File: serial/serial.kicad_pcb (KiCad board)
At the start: 2 copper layers, 73.7 x 56.1 mm, 36 parts, among them J1 Conn_02x20_Odd_Even, J2 D-SUB Male 9 pins, U1 74LS30, U2 74LS02, U3 74LS00, U4 MC6850, U5 CD4060BE, U6 MAX232, Y1 4.0Mhz

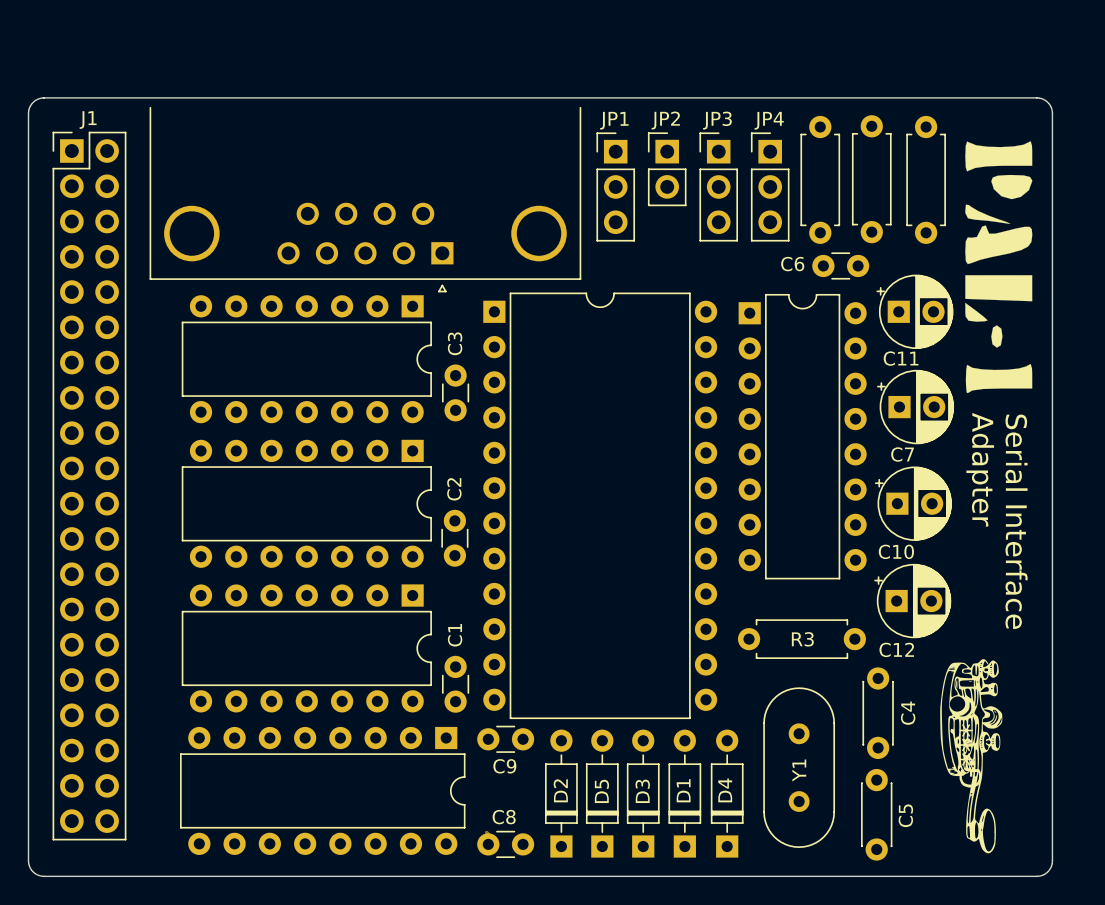
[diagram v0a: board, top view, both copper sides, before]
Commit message: Add TTL header
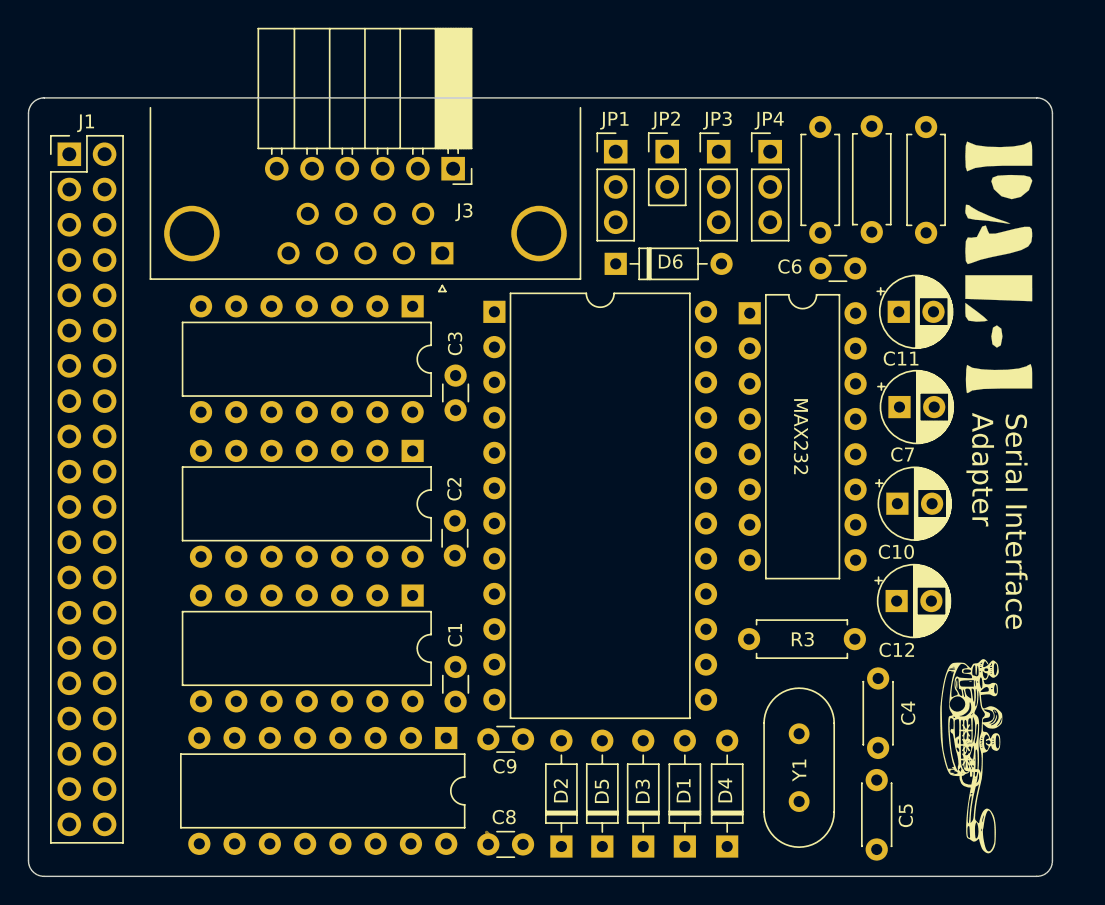
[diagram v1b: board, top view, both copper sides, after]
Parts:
- added D6: 1N4148, Diode_THT:D_DO-35_SOD27_P7.62mm_Horizontal, F.Cu at (142.0, 82.7)
- added J3: Conn_TTL, Connector_PinSocket_2.54mm:PinSocket_1x06_P2.54mm_Horizontal, F.Cu at (130.3, 75.9)
- moved J1 0.30 mm to (102.6, 74.8)
- moved C6 0.27 mm to (156.7, 83.0)
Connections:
- net Net-(U4-Pad2) renamed /Rx_D
- net Net-(U4-Pad24) renamed /CTS#
- net Net-(U4-Pad5) renamed /RTS#
- net Net-(U4-Pad6) renamed /Tx_D
- JP1 pad 2: A1 -> Net-(D6-Pad1)
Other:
- board text added: "MAX232"

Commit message: Minor improvements
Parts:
- removed D6: 1N4148, Diode_THT:D_DO-35_SOD27_P7.62mm_Horizontal
- removed the R2 at (160.4, 80.4)
- C7: renamed from C4; value 33p -> 33pF
- C8: renamed from C5; value 100p -> 100pF
- J3: value Conn_TTL -> Conn_01x06_Male; footprint Connector_PinSocket_2.54mm:PinSocket_1x06_P2.54mm_Horizontal -> Connector_PinHeader_2.54mm:PinHeader_1x06_P2.54mm_Horizontal
- U3: value 74LS00 -> 74LS02
- moved J3 13.1 mm to (117.2, 76.1), turned to 90 degrees
- moved U3 10.5 mm to (127.4, 96.2)
- moved U2 10.4 mm to (127.4, 85.8)
- moved R1 2.39 mm to (162.0, 80.4)
- moved R2 1.91 mm to (158.6, 80.4)
- moved JP1 0.49 mm to (142.3, 74.3)
- moved JP4 0.49 mm to (153.5, 74.3)
- moved JP2 0.49 mm to (146.1, 74.3)
- moved JP3 0.49 mm to (149.8, 74.3)
- moved U6 0.10 mm to (151.6, 86.2)
- renumbered C6 to C4, C9 to C5, C8 to C6, C7 to C9, R3 to R1, R4 to R2
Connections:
- J3 pad 2: /CTS# -> /RTS#
- J3 pad 4: /Tx_D -> /Rx_D
- J3 pad 5: /Rx_D -> /Tx_D
- J3 pad 6: /RTS# -> /CTS#
- JP1 pad 2: Net-(D6-Pad1) -> Net-(JP1-Pad2)
- JP1 pad 3: Net-(JP1-Pad3) -> A1
- U1 pad 1: Net-(JP1-Pad1) -> Net-(JP1-Pad2)
- U2 pad 2: Net-(JP1-Pad3) -> GND
- U3 pad 1: A6 -> Net-(U1-Pad6)
- U3 pad 10: A10 -> Net-(JP1-Pad1)
- U3 pad 11: Net-(U1-Pad11) -> GND
- U3 pad 12: Net-(U3-Pad12) -> GND
- U3 pad 13: Net-(U3-Pad12) -> unconnected-(U3-Pad13)
- U3 pad 2: A7 -> A6
- U3 pad 3: Net-(U3-Pad3) -> A7
- U3 pad 4: Net-(U3-Pad3) -> Net-(U1-Pad11)
- U3 pad 5: Net-(U3-Pad3) -> A9
- U3 pad 6: Net-(U1-Pad6) -> A10
- U3 pad 8: Net-(U3-Pad12) -> A1
- U3 pad 9: A9 -> A1

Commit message: Route pcb
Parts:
- removed the C7 at (160.9, 112.6)
- removed the C8 at (160.8, 124.9)
- removed the J2 at (129.5, 81.9)
- removed the R1 at (162.0, 80.4)
- removed the R1 at (159.2, 109.7)
- removed the U3 at (127.4, 96.2)
- added C12: 33pF, Capacitor_THT:C_Disc_D3.0mm_W1.6mm_P2.50mm, F.Cu at (130.1, 124.2)
- added C13: 33pF, Capacitor_THT:C_Disc_D3.0mm_W1.6mm_P2.50mm, F.Cu at (145.1, 121.6)
- added C4: 0.1uF, Capacitor_THT:C_Disc_D3.0mm_W1.6mm_P2.50mm, F.Cu at (128.0, 101.0)
- added D6: 1N4148, Diode_THT:D_DO-35_SOD27_P7.62mm_Horizontal, F.Cu at (155.2, 111.0)
- added J3: DB9_Male, Connector_Dsub:DSUB-9_Male_Horizontal_P2.77x2.84mm_EdgePinOffset7.70mm_Housed_MountingHolesOffset9.12mm, F.Cu at (129.2, 81.8)
- added R1: 2K2, Resistor_THT:R_Axial_DIN0207_L6.3mm_D2.5mm_P7.62mm_Horizontal, F.Cu at (141.4, 117.5)
- added R3: 2K7, Resistor_THT:R_Axial_DIN0207_L6.3mm_D2.5mm_P7.62mm_Horizontal, F.Cu at (130.6, 95.7)
- added R4: 2K2, Resistor_THT:R_Axial_DIN0207_L6.3mm_D2.5mm_P7.62mm_Horizontal, F.Cu at (130.6, 92.4)
- added R5: 2K2, Resistor_THT:R_Axial_DIN0207_L6.3mm_D2.5mm_P7.62mm_Horizontal, F.Cu at (130.6, 89.2)
- added R6: 2K2, Resistor_THT:R_Axial_DIN0207_L6.3mm_D2.5mm_P7.62mm_Horizontal, F.Cu at (130.6, 85.9)
- added R7: 2K2, Resistor_THT:R_Axial_DIN0207_L6.3mm_D2.5mm_P7.62mm_Horizontal, F.Cu at (132.3, 74.1)
- added U4: 74LS08, Package_DIP:DIP-14_W7.62mm, F.Cu at (124.5, 95.9)
- added U6: 74LS04, Package_DIP:DIP-14_W7.62mm, F.Cu at (124.5, 116.6)
- JP2: value Jumper_2_Open -> Conn_02x09_Odd_Even; footprint Connector_PinHeader_2.54mm:PinHeader_1x02_P2.54mm_Vertical -> Connector_PinHeader_2.54mm:PinHeader_2x09_P2.54mm_Vertical
- JP3, JP4: value Jumper_3_Bridged12 -> Jumper_2_Open; footprint Connector_PinHeader_2.54mm:PinHeader_1x03_P2.54mm_Vertical -> Connector_PinHeader_2.54mm:PinHeader_1x02_P2.54mm_Vertical
- moved C7 58.9 mm to (163.9, 73.0), turned to 0 degrees
- moved R2 33.7 mm to (130.6, 99.0), turned to 0 degrees
- moved JP2 33.6 mm to (141.7, 107.6), turned to 90 degrees
- moved JP1 32.1 mm to (133.1, 105.1), turned to 90 degrees
- moved C6 29.7 mm to (145.1, 119.0)
- moved JP3 28.6 mm to (159.5, 101.2), turned to 90 degrees
- moved C1 28.2 mm to (135.7, 101.9)
- moved JP4 23.9 mm to (159.5, 97.4), turned to 90 degrees
- moved G*** 22.3 mm to (171.1, 105.1)
- moved C9 20.6 mm to (169.6, 80.7)
- moved Y1 20.4 mm to (134.9, 122.4), turned to 0 degrees
- moved U2 19.8 mm to (148.2, 124.2), turned to 90 degrees
- moved C8 19.6 mm to (169.6, 74.7)
- moved D5 17.8 mm to (155.2, 113.9), turned to 0 degrees
- moved D1 16.5 mm to (134.5, 113.9), turned to 0 degrees
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- renumbered C4 to C1, C11 to C10, C12 to C11, C5 to C2, C1 to C3, C2 to C5, C3 to C6, C6 to C7, C9 to C8, C10 to C9, J3 to J2, U4 to U1, U5 to U2, U1 to U3, U2 to U5, U6 to U7
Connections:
- C10 pad 1: Net-(C11-Pad1) -> Net-(C10-Pad1)
- D3 pad 2: Net-(D1-Pad2) -> Net-(D3-Pad2)
- D5 pad 2: Net-(D2-Pad2) -> Net-(D5-Pad2)
- J2 pad 2: /RTS# -> Net-(J2-Pad2)
- J2 pad 4: /Rx_D -> Net-(J2-Pad4)
- J2 pad 5: /Tx_D -> Net-(J2-Pad5)
- J2 pad 6: /CTS# -> Net-(J2-Pad6)
- JP1 pad 1: Net-(JP1-Pad1) -> A1
- JP1 pad 3: A1 -> Net-(JP1-Pad3)
- JP2 pad 1: Net-(JP2-Pad1) -> Net-(D1-Pad2)
- JP2 pad 2: IRQ -> Net-(JP2-Pad10)
- JP3 pad 1: Net-(D4-Pad1) -> Net-(JP3-Pad1)
- JP3 pad 2: CLK -> IRQ
- JP4 pad 1: Net-(D1-Pad2) -> Net-(C10-Pad1)
- JP4 pad 2: Net-(D4-Pad2) -> Net-(JP4-Pad2)
- R2 pad 1: Net-(D4-Pad2) -> Net-(JP2-Pad10)
- U1 pad 10: A3 -> A5
- U1 pad 14: PHI2 -> PHI1
- U1 pad 7: Net-(JP2-Pad1) -> Net-(JP3-Pad1)
- U1 pad 8: A5 -> A3
- U2 pad 10: Net-(C7-Pad2) -> unconnected-(U2-Pad10)
- U2 pad 11: Net-(C8-Pad2) (its old number) -> Net-(C13-Pad2)
- U2 pad 12: Net-(D4-Pad2) -> Net-(JP2-Pad10)
- U2 pad 13: unconnected-(U5-Pad13) -> Net-(D6-Pad1)
- U3 pad 1: Net-(JP1-Pad2) -> Net-(U3-Pad1)
- U3 pad 2: Net-(U1-Pad2) -> Net-(U3-Pad2)
- U3 pad 3: Net-(U1-Pad3) -> Net-(U3-Pad3)
- U3 pad 4: Net-(U1-Pad4) -> Net-(U3-Pad4)
- U3 pad 5: Net-(U1-Pad5) -> Net-(U3-Pad5)
- U3 pad 6: Net-(U1-Pad6) -> Net-(U3-Pad5)
- U5 pad 1: Net-(U1-Pad2) -> Net-(U3-Pad1)
- U5 pad 10: Net-(U1-Pad4) -> Net-(U3-Pad3)
- U5 pad 13: Net-(U1-Pad5) -> Net-(U3-Pad4)
- U5 pad 2: GND -> Net-(JP1-Pad2)
- U5 pad 4: Net-(U1-Pad3) -> Net-(U3-Pad2)
- U7 pad 10: /Tx_D -> /RTS#
- U7 pad 11: /RTS# -> /Tx_D
- U7 pad 12: /Rx_D -> /CTS#
- U7 pad 13: RXD -> /CTS
- U7 pad 14: RTS -> /TXD
- U7 pad 2: Net-(C11-Pad1) -> Net-(C10-Pad1)
- U7 pad 7: TXD -> /RTS
- U7 pad 8: CTS -> /RXD
- U7 pad 9: /CTS# -> /Rx_D
- Y1 pad 1: Net-(C8-Pad2) (its old number) -> Net-(C12-Pad2)
- Y1 pad 2: Net-(C7-Pad2) -> Net-(C13-Pad2)
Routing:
- net VCC: track 1.03 -> 182.7 mm, vias 0 -> 1
- net R/~{W}: track 0.00 -> 82.8 mm
- net A1: track 0.00 -> 76.9 mm, vias 0 -> 2
- net D0: track 0.00 -> 75.1 mm
- net PHI1: track 0.00 -> 72.0 mm
- net /CTS: track 0.00 -> 71.7 mm
- net IRQ: track 0.00 -> 70.5 mm
- net D2: track 0.00 -> 70.5 mm
- net D1: track 0.00 -> 68.7 mm
- net D4: track 0.00 -> 67.5 mm
- net Net-(U1-Pad9): track 0.00 -> 65.7 mm
- net D3: track 0.00 -> 64.3 mm
- net D5: track 0.00 -> 63.5 mm
- net D6: track 0.00 -> 61.6 mm
- net A5: track 0.00 -> 60.8 mm
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- added copper zone on B.Cu, net GND
- added copper zone on F.Cu, net GND
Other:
- board size 73.7 x 56.1 mm -> 75.5 x 56.1 mm
- board text added: "74LS02"
- board text added: "74LS04"
- board text added: "74LS08"
- board text added: "74LS30"
- board text added: "CD4060B"
- board text added: "MC6850"
- board text added: "Serial Interface"
- board text removed: "Serial Interface Adapter"

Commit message: Routing improvements
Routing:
- net Net-(U3-Pad5): track 16.1 -> 31.3 mm
- net GND: track 53.2 -> 38.2 mm, vias 3 -> 0
- net /CTS#: track 50.6 -> 63.0 mm
- net /TXD: track 60.4 -> 50.4 mm, vias 2 -> 1
- net Net-(JP1-Pad2): track 34.8 -> 42.9 mm
- net Net-(C13-Pad2): track 58.8 -> 51.2 mm
- net A1: track 76.9 -> 80.9 mm, vias 2 -> 0
- net /RXD: track 44.6 -> 41.3 mm, vias 2 -> 1
- net Net-(C10-Pad1): track 37.4 -> 34.4 mm
- net Net-(U3-Pad11): track 34.9 -> 37.7 mm
- net Net-(U3-Pad3): track 27.9 -> 30.4 mm
- net Net-(J2-Pad4): track 18.8 -> 17.1 mm
- net /RTS: track 49.1 -> 50.7 mm
- net Net-(U3-Pad4): track 16.2 -> 17.8 mm
- net A12: track 34.6 -> 36.1 mm
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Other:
- board text added: "PAL-1 logo used with kind permission of Liu Ganning"
- board text added: "Plastic Objects Limited 2022 Rev 1.0A"

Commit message: Minor improvements
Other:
- board text added: "1 2 3 4 5 6 7 8 9 ~{- - x - x x - - x} - x - x x - - x - x - x x - - x - -"
- board text added: "9600: 19200: 38400:"
- board text added: "Clk_Config [J2]"
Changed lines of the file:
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@@
     (effects (font (size 1.27 1.27) (thickness 0.254)) (justify left mirror))
   )
-  (gr_text "PAL-1 logo used with kind\npermission of Liu Ganning" (at 144.6022 102.362 270) (layer "B.SilkS")
+  (gr_text "PAL-1 logo used with kind\npermission of Liu Ganning" (at 162.7124 95.5548 270) (layer "B.SilkS")
     (effects (font (size 1.016 1.016) (thickness 0.254)) (justify left mirror))
+  )
+  (gr_text "Clk_Config [J2]" (at 153.3476 102.056495 270) (layer "B.SilkS")
+    (effects (font (size 1 1) (thickness 0.15)) (justify left mirror))
+  )
+  (gr_text "1 2 3 4 5 6 7 8 9\n~{- - x - x x - - x}\n- x - x x - - x -\nx - x x - - x - -" (at 148.6916 87.8586 270) (layer "B.SilkS")
+    (effects (font (size 1 1) (thickness 0.15)) (justify mirror))
+  )
+  (gr_text "9600:\n19200:\n38400:" (at 147.8866 96.4184 270) (layer "B.SilkS")
+    (effects (font (size 1 1) (thickness 0.15)) (justify right mirror))
   )
   (gr_text "MAX232" (at 162.56 84.8106 270) (layer "F.SilkS")
@@
     )
   )
+  (group "" (id be7fa36e-76d0-45aa-8e70-7b6a33824775)
+    (members
+      b90f2dfd-9639-4bac-9825-9f33089900c6
+      ddbf1831-bd5c-4862-80a4-a697cd270798
+    )
+  )
   (group "" (id d61ebff9-2162-495b-9d27-506fd4e99b7a)
     (members
@@
     )
   )
+  (group "" (id ddbf1831-bd5c-4862-80a4-a697cd270798)
+    (members
+      f1cdc1e3-579a-49cb-b214-bbcfabf1e8e7
+      f5085a91-2c3d-4f5c-900f-9ea6af63a392
+    )
+  )
